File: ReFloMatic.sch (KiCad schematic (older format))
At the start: 0 parts

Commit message: Started schematic.  Wired up MAX31855 and TFT connector.
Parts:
- added C1, C? (x2): .01uF, symbol C_Small
- added C?: 10uF, symbol C_Small
- added CON?: BARREL_JACK, symbol BARREL_JACK
- added DS?: ER-TFT028-4, symbol ER-TFT028-4
- added P1: PROG, symbol CONN_02X03
- added P2: THERMOCOUPLE, symbol CONN_01X02
- added P?: DOOR_SERVO, symbol CONN_01X03
- added R1, R2: 470, symbol R
- added R? (x4): 220, symbol R
- added U1: STM32F030C, symbol STM32F030C
- added U2: MAX31855KASA, SO-8, symbol MAX31855KASA
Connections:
- new net: C1.2, R2.1, U2.2 (T-)
- new net: C1.1, R1.1, U2.3 (T+)
- new net: P2.1 (P1), R1.2
- new net: P2.2 (P2), R2.2
- new net: DS?.2 (LED1A), R?.1
- new net: DS?.3 (LED2A), R?.1
- new net: DS?.4 (LED3A), R?.1
- new net: DS?.5 (LED4A), R?.1
- new net +3V3: C?.2, C?.2, C?.2, DS?.35 (RD), DS?.40 (VDDI), DS?.41 (VDDI), DS?.42 (VCI), DS?.7 (IM1), DS?.8 (IM2), DS?.9 (IM3), P1.2 (P2), R?.2, R?.2, R?.2, R?.2, U2.4 (VCC)
- new net +5V: CON?.1, P?.2 (P2)
- new net GND: C?.1, C?.1, C?.1, CON?.2, CON?.3, DS?.1 (LEDK), DS?.11 (VSYNC), DS?.12 (HSYNC), DS?.13 (DOTCLK), DS?.14 (DE), DS?.15 (DB17), DS?.16 (DB16), DS?.17 (DB15), DS?.18 (DB14), DS?.19 (DB13), DS?.20 (DB12), DS?.21 (DB11), DS?.22 (DB10), DS?.23 (DB9), DS?.24 (DB8), DS?.25 (DB7), DS?.26 (DB6), DS?.27 (DB5), DS?.28 (DB4), DS?.29 (DB3), DS?.30 (DB2), DS?.31 (DB1), DS?.32 (DB0), DS?.43 (GND), DS?.48 (GND), DS?.49 (GND), DS?.50 (GND), DS?.6 (IM0), P1.6 (P6), P?.3 (P3), U2.1 (GND)
- new net MAX_MISO: U2.7 (SO)
- new net MAX_SCK: U2.5 (SCK)
- new net SERVO_PWM: P?.1 (P1)
- new net SWCLK: P1.3 (P3), U1.37 (PA14_SWCLK)
- new net SWDIO: P1.1 (P1), U1.34 (PA13_SWDIO)
- new net TFT_MISO: DS?.33 (SDO)
- new net TFT_MOSI: DS?.34 (SDI)
- new net TFT_SCK: DS?.37 (SCL)
- new net TFT_TP_X+: DS?.44 (X+(XR))
- new net TFT_TP_X-: DS?.46 (X-(XL))
- new net TFT_TP_Y+: DS?.45 (Y+(YD))
- new net TFT_TP_Y-: DS?.47 (Y-(YU))
- new net TFT_WR: DS?.36 (WR)
- new net UART_RX: P1.4 (P4)
- new net UART_TX: P1.5 (P5)
- new net ~MAX_CS: U2.6 (~CS~)
- new net ~TFT_CS: DS?.38 (~CS)
- new net ~TFT_RS: DS?.10 (~RESET)
- no-connect marks 0 -> 1

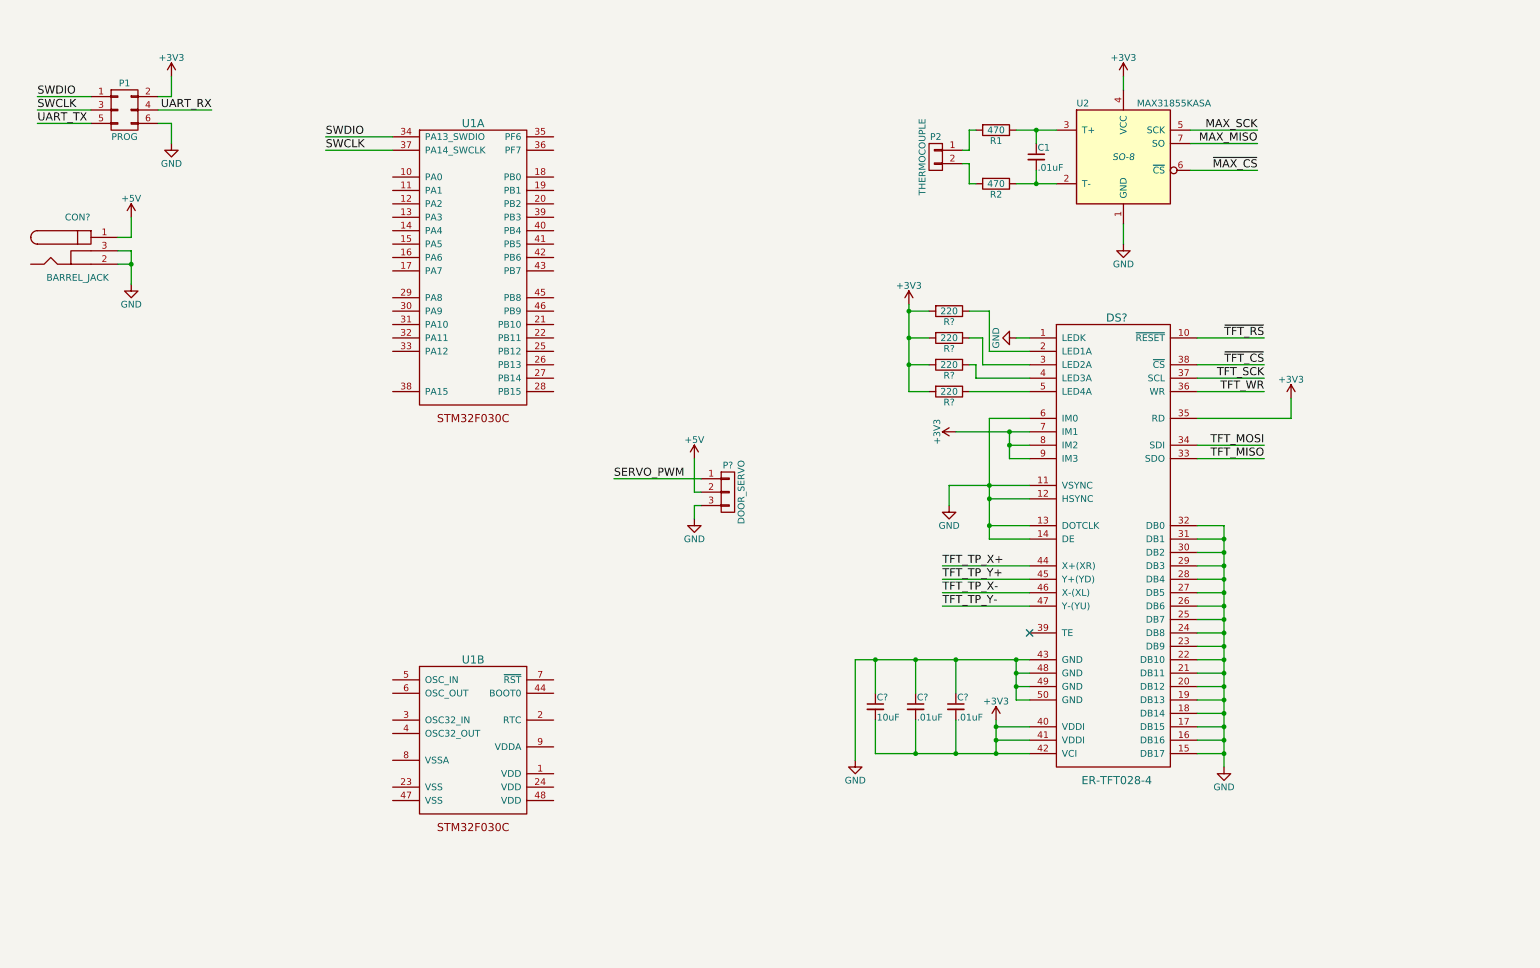
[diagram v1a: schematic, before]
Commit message: Added buzzer and oven connector.
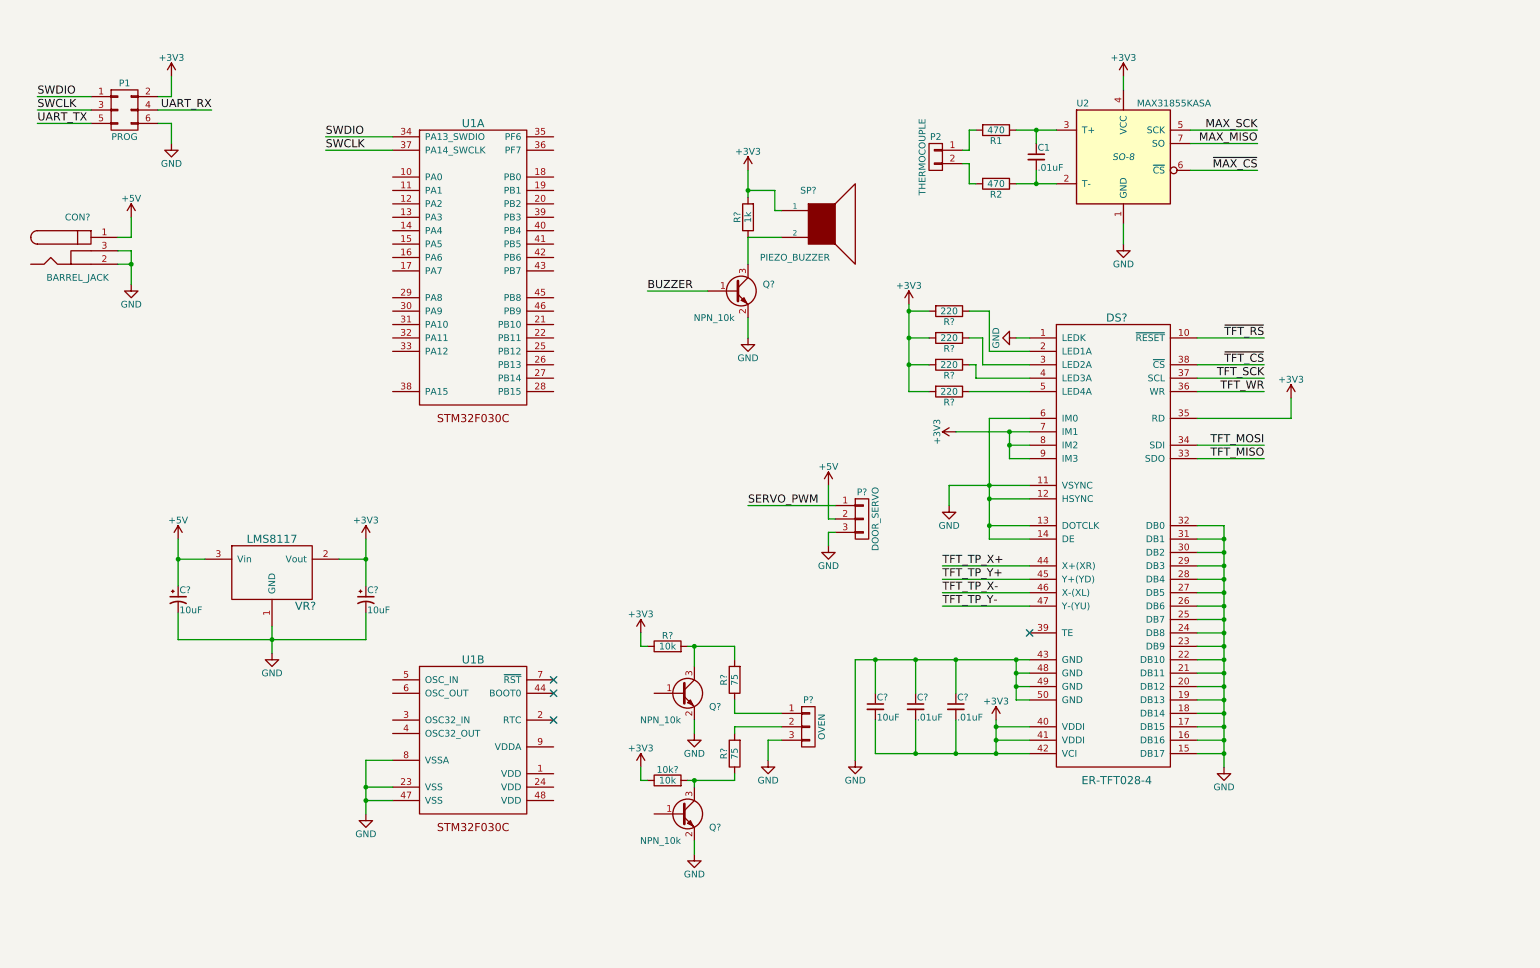
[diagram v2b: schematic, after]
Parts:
- added 10k?, R?: 10k, symbol R
- added C? (x2): 10uF, symbol CP1_Small
- added P?: OVEN, symbol CONN_01X03
- added Q? (x3): NPN_10k, symbol Q_NPN_BEC
- added R?: 1k, symbol R
- added R? (x2): 75, symbol R
- added SP?: PIEZO_BUZZER, symbol SPEAKER
- added VR?: LMS8117, symbol LMS8117
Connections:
- net +3V3: now also 10k?.1, C?.1, R?.1, R?.2, SP?.1, VR?.2 (Vout)
- net +5V: now also C?.1, VR?.3 (Vin)
- net GND: now also U1.23 (VSS), U1.47 (VSS), U1.8 (VSSA), C?.2, C?.2, P?.3 (P3), Q?.2 (E), Q?.2 (E), Q?.2 (E), VR?.1 (GND)
- new net: Q?.3 (C), R?.1, SP?.2
- new net: P?.1 (P1), R?.1
- new net: P?.2 (P2), R?.2
- new net: Q?.3 (C), R?.2, R?.2
- new net: 10k?.2, Q?.3 (C), R?.1
- new net BUZZER: Q?.1 (B)
- no-connect marks 1 -> 4
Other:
- moved on the sheet: P?

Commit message: Finished Rev. A schematic.
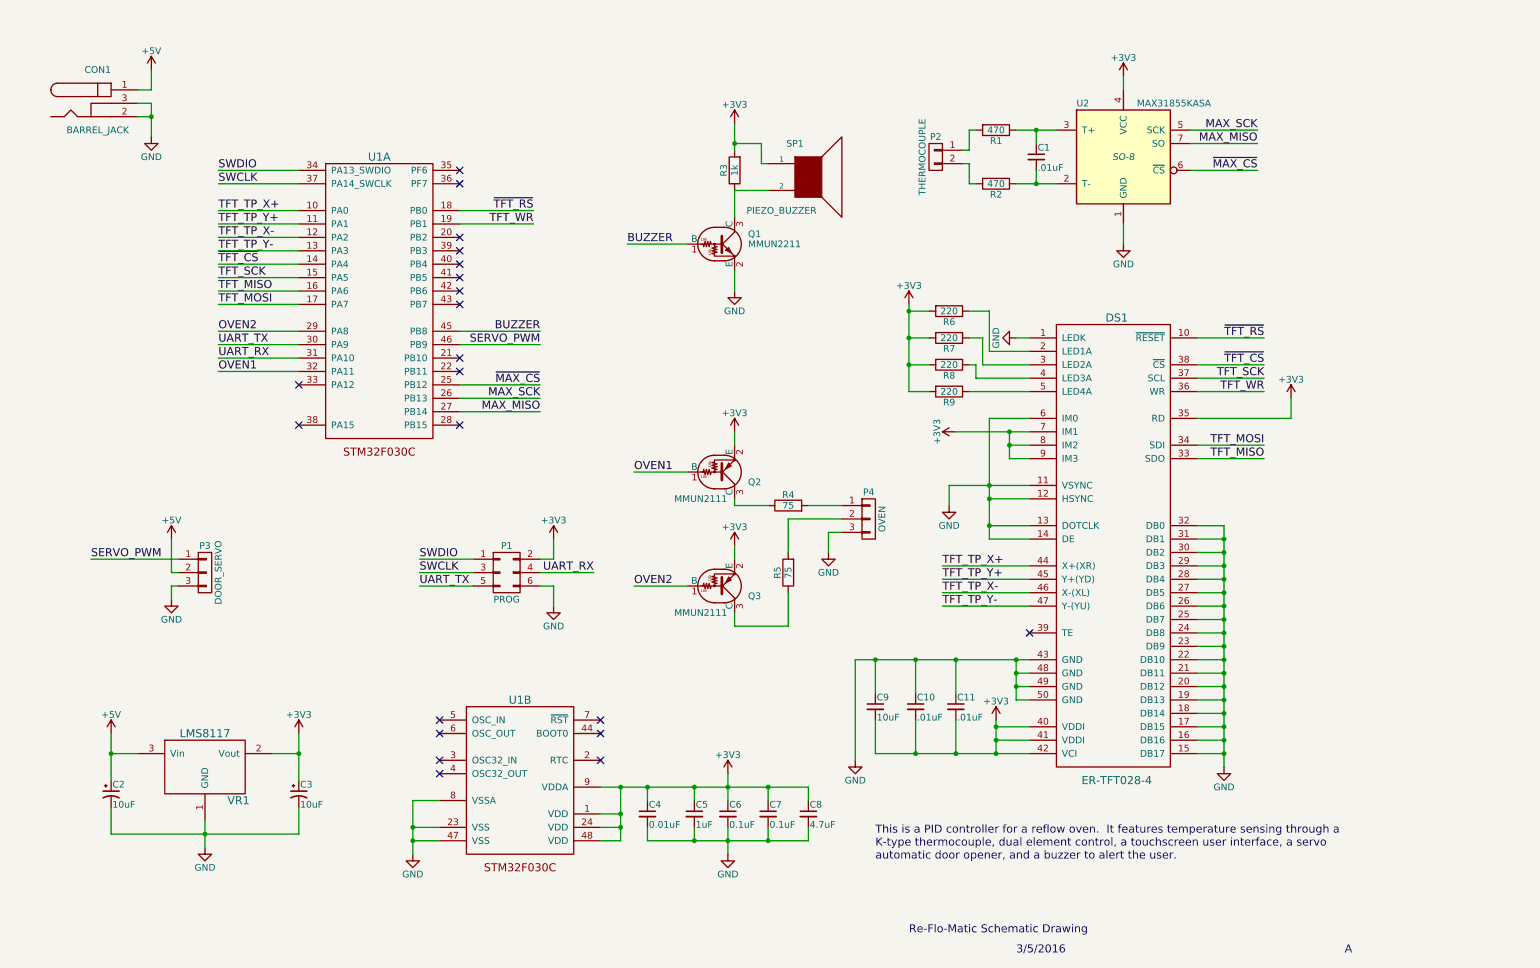
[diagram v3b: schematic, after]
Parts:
- removed 10k?, R?: 10k, symbol R
- removed Q? (x3): NPN_10k, symbol Q_NPN_BEC
- added C4: 0.01uF, symbol C_Small
- added C5: 1uF, symbol C_Small
- added C6, C7: 0.1uF, symbol C_Small
- added C8: 4.7uF, symbol C_Small
- added Q1: MMUN2211, symbol DTC114E
- added Q2, Q3: MMUN2111, symbol DTA114E
- gave numbers to parts that had none: 18
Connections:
- net +3V3: now also U1.1 (VDD), U1.24 (VDD), U1.48 (VDD), U1.9 (VDDA), C4.1, C5.1, C6.1, C7.1, C8.1, Q2.2 (E), Q3.2 (E)
- net BUZZER: now also U1.45 (PB8), Q1.1 (B)
- net GND: now also C4.2, C5.2, C6.2, C7.2, C8.2, Q1.2 (E)
- net MAX_MISO: now also U1.27 (PB14)
- net MAX_SCK: now also U1.26 (PB13)
- net SERVO_PWM: now also U1.46 (PB9)
- net TFT_MISO: now also U1.16 (PA6)
- net TFT_MOSI: now also U1.17 (PA7)
- net TFT_SCK: now also U1.15 (PA5)
- net TFT_TP_X+: now also U1.10 (PA0)
- net TFT_TP_X-: now also U1.12 (PA2)
- net TFT_TP_Y+: now also U1.11 (PA1)
- net TFT_TP_Y-: now also U1.13 (PA3)
- net TFT_WR: now also U1.19 (PB1)
- net UART_RX: now also U1.31 (PA10)
- net UART_TX: now also U1.30 (PA9)
- net ~MAX_CS: now also U1.25 (PB12)
- net ~TFT_CS: now also U1.14 (PA4)
- net ~TFT_RS: now also U1.18 (PB0)
- net OVEN2: now reaches U1.29 (PA8)
- net OVEN2: now also Q3.1 (B)
- net OVEN1: now reaches U1.32 (PA11)
- net OVEN1: now also Q2.1 (B)
- net at R3.1, SP1.2: now also Q1.3 (C)
- net at P4.1 (P1): now also R4.2; no longer R4.1
- net at R5.1: now also Q3.3 (C)
- new net: Q2.3 (C), R4.1
- no-connect marks 4 -> 21
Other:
- note added: "3/5/2016"
- note added: "A"
- note added: "Re-Flo-Matic Schematic Drawing"
- note added: "This is a PID controller for a reflow oven. It features temperature sensing through a\nK-type thermocouple, dual element control, a touchscreen user interface, a servo\nautomatic door opener, and a buzzer to alert the user."
- moved on the sheet: C2, C3, CON1, P1, P3, P4, R3, R4, R5, SP1, U1A, U1B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

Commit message: Started assigning component footprints.
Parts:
- C1, C10, C11, C4, C5, C6, C7: footprint (none) -> Capacitors_SMD:C_0805_HandSoldering
- CON1: footprint (none) -> Barrel_Jacks:CONN-POWER-JACK-SMD-2.1X5.5MM
- Q1, Q2, Q3: footprint (none) -> TO_SOT_Packages_SMD:SOT-23_Handsoldering
- R1, R2, R3, R4, R5, R6, R7, R8, R9: footprint (none) -> Resistors_SMD:R_0805_HandSoldering
- U1: footprint (none) -> Housings_QFP:LQFP-48_7x7mm_Pitch0.5mm
- U2: footprint SO-8 -> Power_Integrations:SO-8
- VR1: footprint (none) -> TO_SOT_Packages_SMD:SOT-223
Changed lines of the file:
@@
 F 0 "U1" H 3400 3500 60  0000 C CNN
 F 1 "STM32F030C" H 3400 1200 60  0001 C CNN
-F 2 "" H 1800 2450 60  0000 C CNN
+F 2 "Housings_QFP:LQFP-48_7x7mm_Pitch0.5mm" H 1800 2450 60  0001 C CNN
 F 3 "" H 1800 2450 60  0000 C CNN
 	1    3400 2600
@@
 F 0 "U1" H 4450 7550 60  0000 C CNN
 F 1 "STM32F030C" H 4450 5250 60  0001 C CNN
-F 2 "" H 2850 6500 60  0000 C CNN
+F 2 "Housings_QFP:LQFP-48_7x7mm_Pitch0.5mm" H 2850 6500 60  0001 C CNN
 F 3 "" H 2850 6500 60  0000 C CNN
 	2    4450 6650
@@
 F 0 "P1" H 4350 5000 50  0000 C CNN
 F 1 "PROG" H 4350 4600 50  0000 C CNN
-F 2 "" H 4350 3600 50  0000 C CNN
+F 2 "" H 4350 3600 50  0001 C CNN
 F 3 "" H 4350 3600 50  0000 C CNN
 	1    4350 4800
@@
 F 0 "U2" H 8600 2100 50  0000 L CNN
 F 1 "MAX31855KASA" H 9050 2100 50  0000 L CNN
-F 2 "SO-8" H 8950 1700 50  0000 C CIN
+F 2 "Power_Integrations:SO-8" H 8950 1700 50  0000 C CIN
 F 3 "" H 8950 1700 50  0000 C CNN
 	1    8950 1700
@@
 F 0 "C1" H 8310 1770 50  0000 L CNN
 F 1 ".01uF" H 8310 1620 50  0000 L CNN
-F 2 "" H 8300 1700 50  0000 C CNN
+F 2 "Capacitors_SMD:C_0805_HandSoldering" H 8300 1700 50  0001 C CNN
 F 3 "" H 8300 1700 50  0000 C CNN
 	1    8300 1700
@@
 F 0 "R1" V 8080 1500 50  0000 C CNN
 F 1 "470" V 8000 1500 50  0000 C CNN
-F 2 "" V 7930 1500 50  0000 C CNN
+F 2 "Resistors_SMD:R_0805_HandSoldering" V 7930 1500 50  0001 C CNN
 F 3 "" H 8000 1500 50  0000 C CNN
 	1    8000 1500
@@
 F 0 "R2" V 8080 1900 50  0000 C CNN
 F 1 "470" V 8000 1900 50  0000 C CNN
-F 2 "" V 7930 1900 50  0000 C CNN
+F 2 "Resistors_SMD:R_0805_HandSoldering" V 7930 1900 50  0001 C CNN
 F 3 "" H 8000 1900 50  0000 C CNN
 	1    8000 1900
@@
 F 0 "P2" H 7550 1850 50  0000 C CNN
 F 1 "THERMOCOUPLE" V 7650 1700 50  0000 C CNN
-F 2 "" H 7550 1700 50  0000 C CNN
+F 2 "" H 7550 1700 50  0001 C CNN
 F 3 "" H 7550 1700 50  0000 C CNN
 	1    7550 1700
@@
 F 0 "CON1" H 1300 1550 50  0000 C CNN
 F 1 "BARREL_JACK" H 1300 1100 50  0000 C CNN
-F 2 "" H 1300 1300 50  0000 C CNN
+F 2 "Barrel_Jacks:CONN-POWER-JACK-SMD-2.1X5.5MM" H 1300 1300 50  0001 C CNN
 F 3 "" H 1300 1300 50  0000 C CNN
 	1    1300 1300
@@
 F 0 "P3" H 2100 5000 50  0000 C CNN
 F 1 "DOOR_SERVO" V 2200 4800 50  0000 C CNN
-F 2 "" H 2100 4800 50  0000 C CNN
+F 2 "" H 2100 4800 50  0001 C CNN
 F 3 "" H 2100 4800 50  0000 C CNN
 	1    2100 4800
@@
 F 0 "DS1" H 8900 6300 60  0000 C CNN
 F 1 "ER-TFT028-4" H 8900 2850 60  0000 C CNN
-F 2 "" H 8850 6300 60  0000 C CNN
+F 2 "" H 8850 6300 60  0001 C CNN
 F 3 "" H 8850 6300 60  0000 C CNN
 	1    8900 4600
@@
 F 0 "R6" V 7730 2850 50  0000 C CNN
 F 1 "220" V 7650 2850 50  0000 C CNN
-F 2 "" V 7580 2850 50  0000 C CNN
+F 2 "Resistors_SMD:R_0805_HandSoldering" V 7580 2850 50  0001 C CNN
 F 3 "" H 7650 2850 50  0000 C CNN
 	1    7650 2850
@@
 F 0 "R7" V 7730 3050 50  0000 C CNN
 F 1 "220" V 7650 3050 50  0000 C CNN
-F 2 "" V 7580 3050 50  0000 C CNN
+F 2 "Resistors_SMD:R_0805_HandSoldering" V 7580 3050 50  0001 C CNN
 F 3 "" H 7650 3050 50  0000 C CNN
 	1    7650 3050
@@
 F 0 "R8" V 7730 3250 50  0000 C CNN
 F 1 "220" V 7650 3250 50  0000 C CNN
-F 2 "" V 7580 3250 50  0000 C CNN
+F 2 "Resistors_SMD:R_0805_HandSoldering" V 7580 3250 50  0001 C CNN
 F 3 "" H 7650 3250 50  0000 C CNN
 	1    7650 3250
@@
 F 0 "R9" V 7730 3450 50  0000 C CNN
 F 1 "220" V 7650 3450 50  0000 C CNN
-F 2 "" V 7580 3450 50  0000 C CNN
+F 2 "Resistors_SMD:R_0805_HandSoldering" V 7580 3450 50  0001 C CNN
 F 3 "" H 7650 3450 50  0000 C CNN
 	1    7650 3450
@@
 F 0 "C11" H 7710 5870 50  0000 L CNN
 F 1 ".01uF" H 7710 5720 50  0000 L CNN
-F 2 "" H 7700 5800 50  0000 C CNN
+F 2 "Capacitors_SMD:C_0805_HandSoldering" H 7700 5800 50  0001 C CNN
 F 3 "" H 7700 5800 50  0000 C CNN
 	1    7700 5800
@@
 F 0 "C10" H 7410 5870 50  0000 L CNN
 F 1 ".01uF" H 7410 5720 50  0000 L CNN
-F 2 "" H 7400 5800 50  0000 C CNN
+F 2 "Capacitors_SMD:C_0805_HandSoldering" H 7400 5800 50  0001 C CNN
 F 3 "" H 7400 5800 50  0000 C CNN
 	1    7400 5800
@@
 F 0 "C9" H 7110 5870 50  0000 L CNN
 F 1 "10uF" H 7110 5720 50  0000 L CNN
-F 2 "" H 7100 5800 50  0000 C CNN
+F 2 "" H 7100 5800 50  0001 C CNN
 F 3 "" H 7100 5800 50  0000 C CNN
 	1    7100 5800
@@
 F 0 "VR1" H 2350 6000 60  0000 C CNN
 F 1 "LMS8117" H 2100 6500 60  0000 C CNN
-F 2 "" H 2100 6650 60  0000 C CNN
+F 2 "TO_SOT_Packages_SMD:SOT-223" H 2100 6650 60  0001 C CNN
 F 3 "" H 2100 6650 60  0000 C CNN
 	1    2100 6250
@@
 F 0 "C3" H 2810 6520 50  0000 L CNN
 F 1 "10uF" H 2810 6370 50  0000 L CNN
-F 2 "" H 2800 6450 50  0000 C CNN
+F 2 "" H 2800 6450 50  0001 C CNN
 F 3 "" H 2800 6450 50  0000 C CNN
 	1    2800 6450
@@
 F 0 "C2" H 1410 6520 50  0000 L CNN
 F 1 "10uF" H 1410 6370 50  0000 L CNN
-F 2 "" H 1400 6450 50  0000 C CNN
+F 2 "" H 1400 6450 50  0001 C CNN
 F 3 "" H 1400 6450 50  0000 C CNN
 	1    1400 6450
@@
 F 0 "SP1" H 6500 2100 50  0000 C CNN
 F 1 "PIEZO_BUZZER" H 6400 1600 50  0000 C CNN
-F 2 "" H 6600 1850 50  0000 C CNN
+F 2 "" H 6600 1850 50  0001 C CNN
 F 3 "" H 6600 1850 50  0000 C CNN
 	1    6600 1850
@@
 F 0 "R3" V 6130 1800 50  0000 C CNN
 F 1 "1k" V 6050 1800 50  0000 C CNN
-F 2 "" V 5980 1800 50  0000 C CNN
+F 2 "Resistors_SMD:R_0805_HandSoldering" V 5980 1800 50  0001 C CNN
 F 3 "" H 6050 1800 50  0000 C CNN
 	1    6050 1800
@@
 F 0 "P4" H 7050 4600 50  0000 C CNN
 F 1 "OVEN" V 7150 4400 50  0000 C CNN
-F 2 "" H 7050 4400 50  0000 C CNN
+F 2 "" H 7050 4400 50  0001 C CNN
 F 3 "" H 7050 4400 50  0000 C CNN
 	1    7050 4400
@@
 F 0 "R4" V 6530 4300 50  0000 C CNN
 F 1 "75" V 6450 4300 50  0000 C CNN
-F 2 "" V 6380 4300 50  0000 C CNN
+F 2 "Resistors_SMD:R_0805_HandSoldering" V 6380 4300 50  0001 C CNN
 F 3 "" H 6450 4300 50  0000 C CNN
 	1    6450 4300
@@
 F 0 "R5" V 6530 4800 50  0000 C CNN
 F 1 "75" V 6450 4800 50  0000 C CNN
-F 2 "" V 6380 4800 50  0000 C CNN
+F 2 "Resistors_SMD:R_0805_HandSoldering" V 6380 4800 50  0001 C CNN
 F 3 "" H 6450 4800 50  0000 C CNN
 	1    6450 4800
@@
 F 0 "C4" H 5410 6670 50  0000 L CNN
 F 1 "0.01uF" H 5410 6520 50  0000 L CNN
-F 2 "" H 5400 6600 50  0000 C CNN
+F 2 "Capacitors_SMD:C_0805_HandSoldering" H 5400 6600 50  0001 C CNN
 F 3 "" H 5400 6600 50  0000 C CNN
 	1    5400 6600
@@
 F 0 "C5" H 5760 6670 50  0000 L CNN
 F 1 "1uF" H 5760 6520 50  0000 L CNN
-F 2 "" H 5750 6600 50  0000 C CNN
+F 2 "Capacitors_SMD:C_0805_HandSoldering" H 5750 6600 50  0001 C CNN
 F 3 "" H 5750 6600 50  0000 C CNN
 	1    5750 6600
@@
 F 0 "C6" H 6010 6670 50  0000 L CNN
 F 1 "0.1uF" H 6010 6520 50  0000 L CNN
-F 2 "" H 6000 6600 50  0000 C CNN
+F 2 "Capacitors_SMD:C_0805_HandSoldering" H 6000 6600 50  0001 C CNN
 F 3 "" H 6000 6600 50  0000 C CNN
 	1    6000 6600
@@
 F 0 "C7" H 6310 6670 50  0000 L CNN
 F 1 "0.1uF" H 6310 6520 50  0000 L CNN
-F 2 "" H 6300 6600 50  0000 C CNN
+F 2 "Capacitors_SMD:C_0805_HandSoldering" H 6300 6600 50  0001 C CNN
 F 3 "" H 6300 6600 50  0000 C CNN
 	1    6300 6600
@@
 F 0 "C8" H 6610 6670 50  0000 L CNN
 F 1 "4.7uF" H 6610 6520 50  0000 L CNN
-F 2 "" H 6600 6600 50  0000 C CNN
+F 2 "" H 6600 6600 50  0001 C CNN
 F 3 "" H 6600 6600 50  0000 C CNN
 	1    6600 6600
@@
 F 0 "Q1" H 6150 2425 50  0000 L CNN
 F 1 "MMUN2211" H 6150 2350 50  0000 L CNN
-F 2 "" H 5950 2350 50  0000 L CNN
+F 2 "TO_SOT_Packages_SMD:SOT-23_Handsoldering" H 5950 2350 50  0001 L CNN
 F 3 "" H 5950 2350 50  0000 L CNN
 	1    5950 2350
@@
 F 0 "Q2" H 6150 4125 50  0000 L CNN
 F 1 "MMUN2111" H 5600 4250 50  0000 L CNN
-F 2 "" H 5950 4050 50  0000 L CNN
+F 2 "TO_SOT_Packages_SMD:SOT-23_Handsoldering" H 5950 4050 50  0001 L CNN
 F 3 "" H 5950 4050 50  0000 L CNN
 	1    5950 4050
@@
 F 0 "Q3" H 6150 4975 50  0000 L CNN
 F 1 "MMUN2111" H 5600 5100 50  0000 L CNN
-F 2 "" H 5950 4900 50  0000 L CNN
+F 2 "TO_SOT_Packages_SMD:SOT-23_Handsoldering" H 5950 4900 50  0001 L CNN
 F 3 "" H 5950 4900 50  0000 L CNN
 	1    5950 4900

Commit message: Started assigning components.
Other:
- note added: "TODO\n--------------------------------\n+ Make sure TFT LED resistor values are correct.\n+ Add a transistor to turn TFT LEDs on and off.\n+ Add Micro SD connector to SPI bus.\n+ Make sure piezo resistor is the correct value.\n+ Reverse TFT connector pin order."
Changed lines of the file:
@@
 Text Notes 10600 7650 0    60   ~ 0
 A
+Text Notes 2450 1400 0    60   ~ 0
+TODO\n--------------------------------\n+ Make sure TFT LED resistor values are correct.\n+ Add a transistor to turn TFT LEDs on and off.\n+ Add Micro SD connector to SPI bus.\n+ Make sure piezo resistor is the correct value.\n+ Reverse TFT connector pin order.
 $EndSCHEMATC
